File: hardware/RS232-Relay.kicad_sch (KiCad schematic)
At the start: 45 parts, among them J2 Conn_01x02, J4 Conn_01x09, J5 Conn_01x09, J7 RS232_1, J8 RS232_2, SW2 SW_SPST, SW3 SW_SPST, U1 TEC2-1210WI, U3 PCF8575DBR, U4 MAX3232

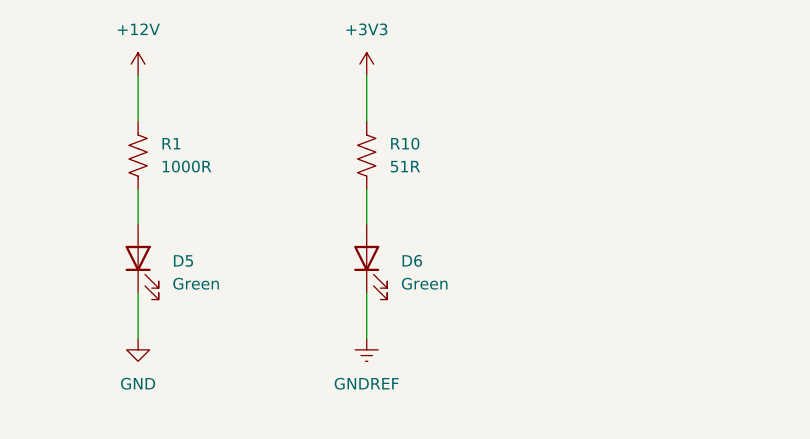
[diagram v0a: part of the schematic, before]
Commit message: Transitioning to more robust circuit
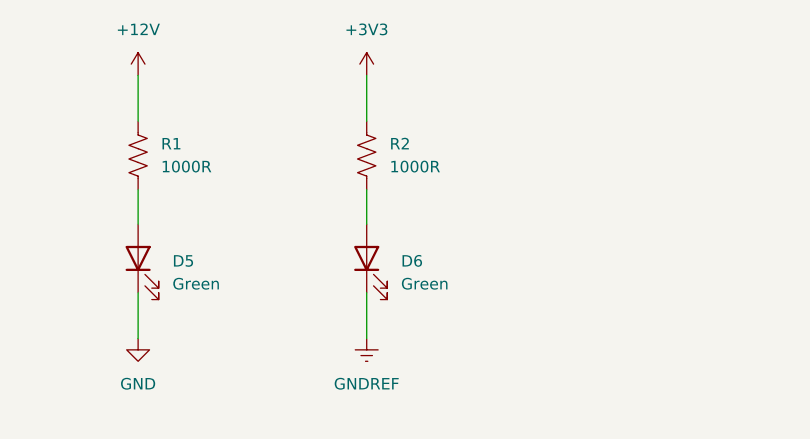
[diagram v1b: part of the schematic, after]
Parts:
- removed R10: 51R, Resistor_SMD:R_0603_1608Metric, symbol Device:R_US
- added R2: 1000R, Resistor_SMD:R_0603_1608Metric, symbol Device:R_US
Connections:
- net +3V3: now also R2.1
- net at D6.2 (A): now also R2.2
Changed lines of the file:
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@@
+	)
+	(symbol
+		(lib_id "Device:R_US")
+		(at 107.95 30.48 0)
+		(unit 1)
+		(exclude_from_sim no)
+		(in_bom yes)
+		(on_board yes)
+		(dnp no)
+		(fields_autoplaced yes)
+		(property "Reference" "R2"
+			(at 110.49 29.2099 0)
+			(effects
+				(font
+					(size 1.27 1.27)
+				)
+				(justify left)
+			)
+		)
+		(property "Value" "1000R"
+			(at 110.49 31.7499 0)
+			(effects
+				(font
+					(size 1.27 1.27)
+				)
+				(justify left)
+			)
+		)
+		(property "Footprint" "Resistor_SMD:R_0603_1608Metric"
+			(at 108.966 30.734 90)
+			(effects
+				(font
+					(size 1.27 1.27)
+				)
+				(hide yes)
+			)
+		)
+		(property "Datasheet" "~"
+			(at 107.95 30.48 0)
+			(effects
+				(font
+					(size 1.27 1.27)
+				)
+				(hide yes)
+			)
+		)
+		(property "Description" "Resistor, US symbol"
+			(at 107.95 30.48 0)
+			(effects
+				(font
+					(size 1.27 1.27)
+				)
+				(hide yes)
+			)
+		)
+		(property "LCSC" "C21190"
+			(at 107.95 30.48 0)
+			(effects
+				(font
+					(size 1.27 1.27)
+				)
+				(hide yes)
+			)
+		)
+		(pin "2"
+		)
+		(pin "1"
+		)
+		(instances
+			(project "RS232-Relay"
+				(path "/6e416d74-c18a-4d9a-a47c-4314aa8f470f"
+					(reference "R2")
+					(unit 1)
+				)
+			)
+		)
 	)
 	(symbol
@@
 					(unit 1)
 				)
-			)
-		)
-	)
-	(symbol
-		(lib_id "Device:R_US")
-		(at 107.95 30.48 180)
-		(unit 1)
-		(exclude_from_sim no)
-		(in_bom yes)
-		(on_board yes)
-		(dnp no)
-		(fields_autoplaced yes)
-		(property "Reference" "R10"
-			(at 110.49 29.2099 0)
-			(effects
-				(font
-					(size 1.27 1.27)
-				)
-				(justify right)
-			)
-		)
-		(property "Value" "51R"
-			(at 110.49 31.7499 0)
-			(effects
-				(font
-					(size 1.27 1.27)
-				)
-				(justify right)
-			)
-		)
-		(property "Footprint" "Resistor_SMD:R_0603_1608Metric"
-			(at 106.934 30.226 90)
-			(effects
-				(font
-					(size 1.27 1.27)
-				)
-				(hide yes)
-			)
-		)
-		(property "Datasheet" "~"
-			(at 107.95 30.48 0)
-			(effects
-				(font
-					(size 1.27 1.27)
-				)
-				(hide yes)
-			)
-		)
-		(property "Description" "Resistor, US symbol"
-			(at 107.95 30.48 0)
-			(effects
-				(font
-					(size 1.27 1.27)
-				)
-				(hide yes)
-			)
-		)
-		(property "LCSC" "C23197"
-			(at 107.95 30.48 90)
-			(effects
-				(font
-					(size 1.27 1.27)
-				)
-				(hide yes)
-			)
-		)
-		(pin "1"
-		)
-		(pin "2"
-		)
-		(instances
-			(project "RS232-Relay"
-				(path "/6e416d74-c18a-4d9a-a47c-4314aa8f470f"
-					(reference "R10")
-					(unit 1)
-				)

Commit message: It could work but it's too big
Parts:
- removed C12, C15: 1uF, Capacitor_SMD:C_0402_1005Metric, symbol Device:C_Small
- removed C13: 0.1uF, Capacitor_SMD:C_0402_1005Metric, symbol Device:C_Small
- removed R4, R8, R9: 4K7, Resistor_SMD:R_0603_1608Metric, symbol Device:R_US
- removed R7: 10K, Resistor_SMD:R_0402_1005Metric, symbol Device:R_US
- removed SW3: SW_SPST, Switch:PTS841, symbol Switch:SW_SPST
- removed TP10: I2C_SCL, TestPoint:TestPoint_Pad_D1.0mm, symbol Connector:TestPoint
- removed TP11: I2C_INT, TestPoint:TestPoint_Pad_D1.0mm, symbol Connector:TestPoint
- removed TP13: BTN_02, TestPoint:TestPoint_Pad_D1.0mm, symbol Connector:TestPoint
- removed TP9: I2C_SDA, TestPoint:TestPoint_Pad_D1.0mm, symbol Connector:TestPoint
- removed U3: PCF8575DBR, Package_SO:SSOP-24_5.3x8.2mm_P0.65mm, symbol Interface_Expansion:PCF8575DBR
- added J1, J3, J6: Conn_01x08, Connector_Phoenix_MSTB:PhoenixContact_MSTBA_2,5_8-G-5,08_1x08_P5.08mm_Horizontal, symbol Connector_Generic:Conn_01x08
- added U16, U3: ULN2003, Package_DIP:DIP-16_W7.62mm_Socket, symbol Transistor_Array:ULN2003
- R1: value 1000R -> 2000R; LCSC C21190 -> C22975
- R2: value 1000R -> 220R; LCSC C21190 -> C22962
- SW2: footprint Switch:PTS841 -> Button_Switch_THT:SW_PUSH_1P1T_6x3.5mm_H4.3_APEM_MJTP1243
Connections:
- net +12V: now also U16.9 (COM), U3.9 (COM); no longer U1.3 (ON/~{OFF})
- net BTN_01: now also J5.3 (Pin_3); no longer J5.8 (Pin_8)
- net GND: now also U1.3 (ON/~{OFF}), J1.2 (Pin_2), J1.4 (Pin_4), J1.6 (Pin_6), J1.8 (Pin_8), J3.2 (Pin_2), J3.4 (Pin_4), J3.6 (Pin_6), J3.8 (Pin_8), J6.2 (Pin_2), J6.4 (Pin_4), J6.6 (Pin_6), J6.8 (Pin_8), U16.8 (GND), U3.8 (GND)
- net UART_2_RX: no longer J5.4 (Pin_4)
- net UART_2_TX: no longer J5.3 (Pin_3)
- net BTN_02 renamed ESP_32_GPIO_22
- net I2C_INT renamed ESP_32_GPIO_05
- net I2C_SCL renamed ESP_32_GPIO_03
- net I2C_SDA renamed ESP_32_GPIO_04
- new net ESP_32_GPIO_15: J5.4 (Pin_4)
- new net ESP_32_GPIO_21: J5.8 (Pin_8)
- new net RELAY_OUT_01: J1.1 (Pin_1)
- new net RELAY_OUT_02: J1.3 (Pin_3)
- new net RELAY_OUT_03: J1.5 (Pin_5)
- new net RELAY_OUT_04: J1.7 (Pin_7)
- new net RELAY_OUT_05: J3.1 (Pin_1)
- new net RELAY_OUT_06: J3.3 (Pin_3)
- new net RELAY_OUT_07: J3.5 (Pin_5)
- new net RELAY_OUT_08: J3.7 (Pin_7)
- new net RELAY_OUT_09: J6.1 (Pin_1)
- new net RELAY_OUT_10: J6.3 (Pin_3)
- new net RELAY_OUT_11: J6.5 (Pin_5)
- new net RELAY_OUT_12: J6.7 (Pin_7)
- new net ULN_ISO_01: U3.1 (I1)
- new net ULN_ISO_02: U3.2 (I2)
- new net ULN_ISO_03: U3.3 (I3)
- new net ULN_ISO_04: U3.4 (I4)
- new net ULN_ISO_05: U3.5 (I5)
- new net ULN_ISO_06: U3.6 (I6)
- new net ULN_ISO_07: U16.1 (I1)
- new net ULN_ISO_08: U16.2 (I2)
- new net ULN_ISO_09: U16.3 (I3)
- new net ULN_ISO_10: U16.4 (I4)
- new net ULN_ISO_11: U16.5 (I5)
- new net ULN_ISO_12: U16.6 (I6)
- new net ULN_RELAY_01: U3.16 (O1)
- new net ULN_RELAY_02: U3.15 (O2)
- new net ULN_RELAY_03: U3.14 (O3)
- new net ULN_RELAY_04: U3.13 (O4)
- new net ULN_RELAY_05: U3.12 (O5)
- new net ULN_RELAY_06: U3.11 (O6)
- new net ULN_RELAY_07: U16.16 (O1)
- new net ULN_RELAY_08: U16.15 (O2)
- new net ULN_RELAY_09: U16.14 (O3)
- new net ULN_RELAY_10: U16.13 (O4)
- new net ULN_RELAY_11: U16.12 (O5)
- new net ULN_RELAY_12: U16.11 (O6)
- no-connect marks 12 -> 6
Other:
- removed sheet Relay-Module
- removed sheet Relay-Module1
- removed sheet Relay-Module2
- added sheet Relay-NO-ISO (Relay-NO-ISO.kicad_sch)
- added sheet Relay-NO-ISO1 (Relay-NO-ISO.kicad_sch)
- added sheet Relay-NO-ISO10 (Relay-NO-ISO.kicad_sch)
- added sheet Relay-NO-ISO11 (Relay-NO-ISO.kicad_sch)
- added sheet Relay-NO-ISO2 (Relay-NO-ISO.kicad_sch)
- added sheet Relay-NO-ISO3 (Relay-NO-ISO.kicad_sch)
- added sheet Relay-NO-ISO4 (Relay-NO-ISO.kicad_sch)
- added sheet Relay-NO-ISO5 (Relay-NO-ISO.kicad_sch)
- added sheet Relay-NO-ISO6 (Relay-NO-ISO.kicad_sch)
- added sheet Relay-NO-ISO7 (Relay-NO-ISO.kicad_sch)
- added sheet Relay-NO-ISO8 (Relay-NO-ISO.kicad_sch)
- added sheet Relay-NO-ISO9 (Relay-NO-ISO.kicad_sch)
- note removed: "Buttons"
- note removed: "Check spacing of this to edge of board"
- note removed: "I2C Pullup"
- note removed: "IO Expansion"
- moved on the sheet: C1, C2, F1, J2, U1

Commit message: Schematic ready
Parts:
- U16, U3: footprint Package_DIP:DIP-16_W7.62mm_Socket -> Package_DIP:DIP-16_W7.62mm_SMDSocket_SmallPads; LCSC (none) -> C2690547
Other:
- added sheet Isolator (untitled.kicad_sch)
- added sheet Isolator1 (untitled.kicad_sch)
- added sheet Isolator2 (untitled.kicad_sch)
- sheet Relay-NO-ISO ports: added none; removed ESP32_IN, ULN_ISOLATOR
- sheet Relay-NO-ISO1 ports: added none; removed ESP32_IN, ULN_ISOLATOR
- sheet Relay-NO-ISO10 ports: added none; removed ESP32_IN, ULN_ISOLATOR
- sheet Relay-NO-ISO11 ports: added none; removed ESP32_IN, ULN_ISOLATOR
- sheet Relay-NO-ISO2 ports: added none; removed ESP32_IN, ULN_ISOLATOR
- sheet Relay-NO-ISO3 ports: added none; removed ESP32_IN, ULN_ISOLATOR
- sheet Relay-NO-ISO4 ports: added none; removed ESP32_IN, ULN_ISOLATOR
- sheet Relay-NO-ISO5 ports: added none; removed ESP32_IN, ULN_ISOLATOR
- sheet Relay-NO-ISO6 ports: added none; removed ESP32_IN, ULN_ISOLATOR
- sheet Relay-NO-ISO7 ports: added none; removed ESP32_IN, ULN_ISOLATOR
- sheet Relay-NO-ISO8 ports: added none; removed ESP32_IN, ULN_ISOLATOR
- sheet Relay-NO-ISO9 ports: added none; removed ESP32_IN, ULN_ISOLATOR
